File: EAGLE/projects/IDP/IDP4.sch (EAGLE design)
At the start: 14 parts, among them IC1 LM348P, M1 IDP_PROTOBOARD, U1 LM393P

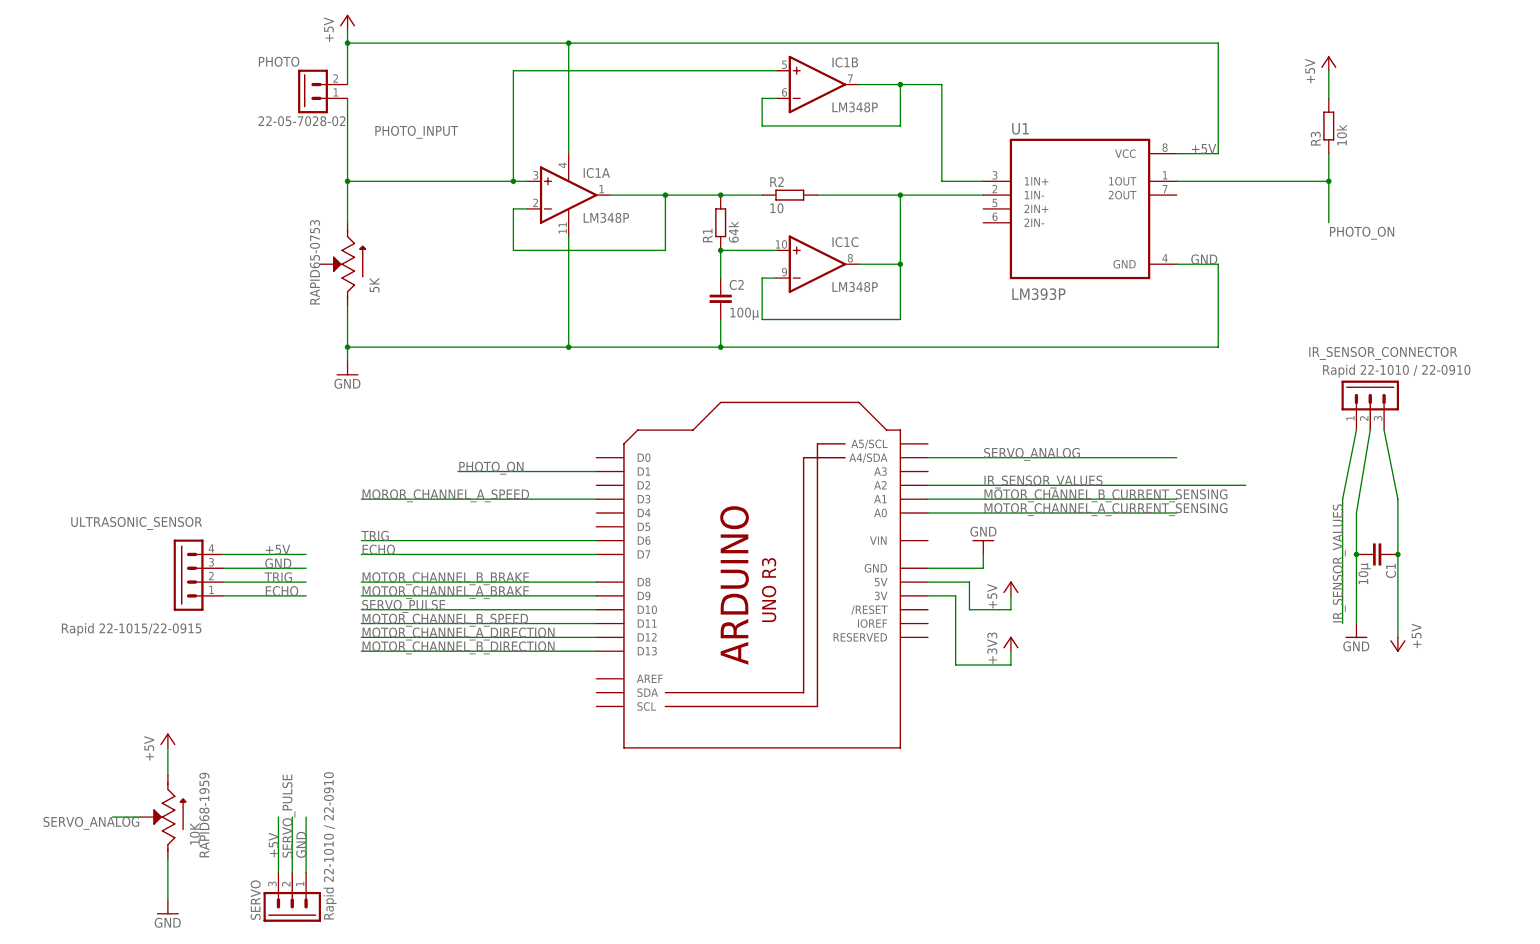
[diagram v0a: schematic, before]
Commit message: Added LED :+1:
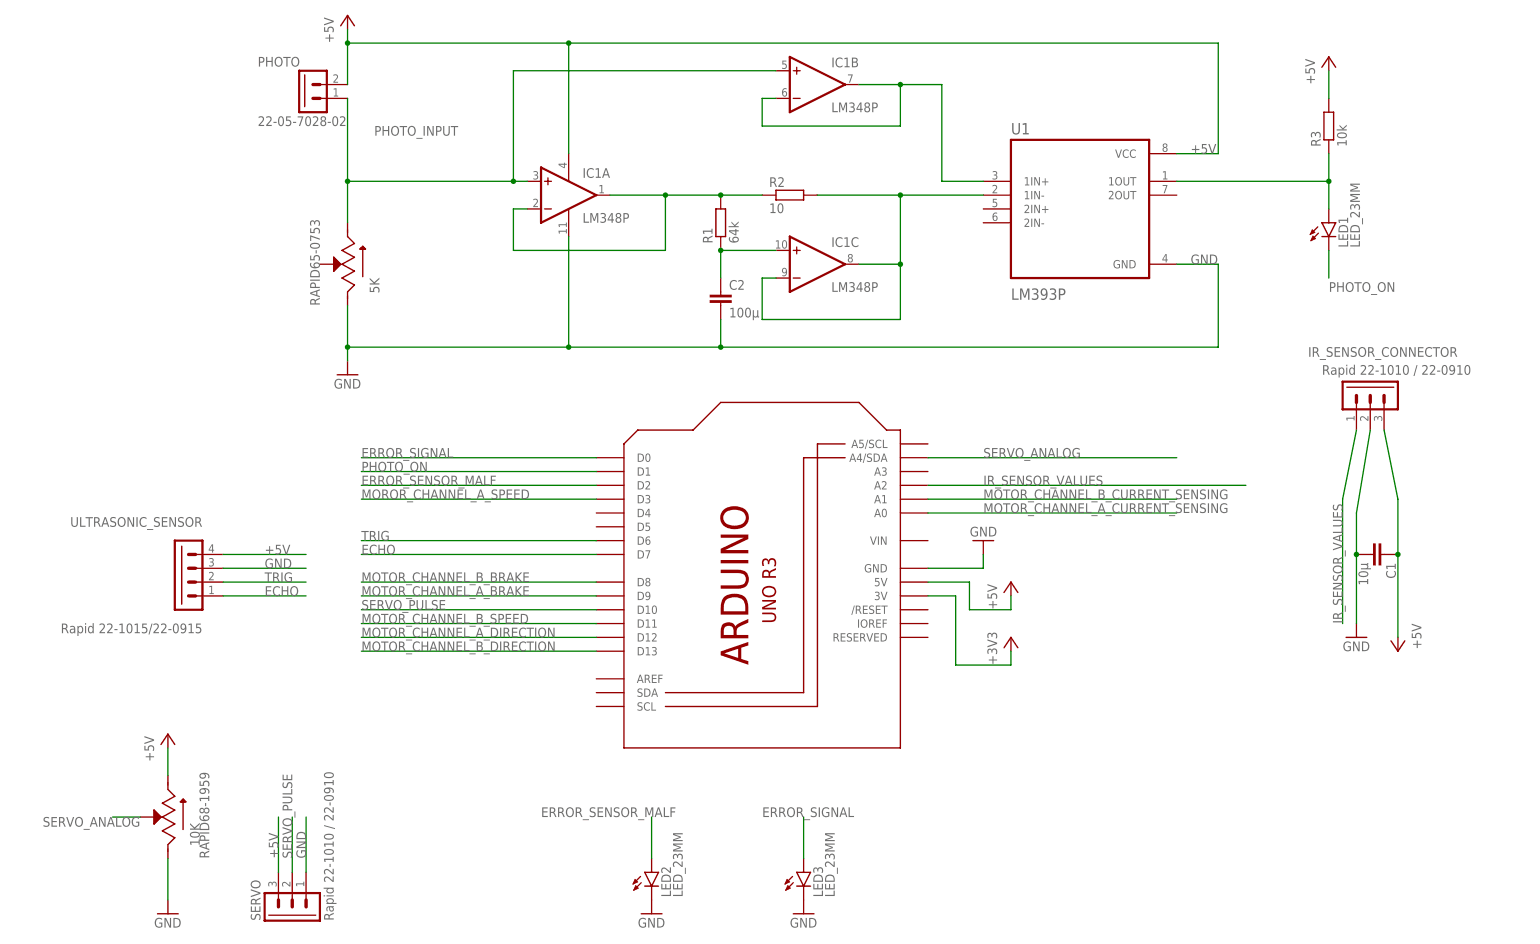
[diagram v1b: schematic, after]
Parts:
- added LED1, LED2, LED3: LED_23MM, IDP_library:LED_23MM
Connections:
- new net ERROR_SENSOR_MALF: LED2.A, M1.D2
- new net ERROR_SIGNAL: LED3.A, M1.D0
- net GND: now also LED2.C, LED3.C
- net PHOTO_ON: now also LED1.A, LED1.C
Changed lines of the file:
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@@
 <grid distance="0.1" unitdist="inch" unit="inch" style="lines" multiple="1" display="no" altdistance="0.01" altunitdist="inch" altunit="inch"/>
 <layers>
-<layer number="1" name="Top" color="4" fill="1" visible="yes" active="no"/>
-<layer number="16" name="Bottom" color="1" fill="1" visible="yes" active="no"/>
-<layer number="17" name="Pads" color="2" fill="1" visible="yes" active="no"/>
-<layer number="18" name="Vias" color="2" fill="1" visible="yes" active="no"/>
-<layer number="19" name="Unrouted" color="6" fill="1" visible="yes" active="no"/>
-<layer number="20" name="Dimension" color="24" fill="1" visible="yes" active="no"/>
-<layer number="21" name="tPlace" color="7" fill="1" visible="yes" active="no"/>
-<layer number="22" name="bPlace" color="7" fill="1" visible="yes" active="no"/>
-<layer number="23" name="tOrigins" color="15" fill="1" visible="yes" active="no"/>
-<layer number="24" name="bOrigins" color="15" fill="1" visible="yes" active="no"/>
-<layer number="25" name="tNames" color="7" fill="1" visible="yes" active="no"/>
-<layer number="26" name="bNames" color="7" fill="1" visible="yes" active="no"/>
-<layer number="27" name="tValues" color="7" fill="1" visible="yes" active="no"/>
-<layer number="28" name="bValues" color="7" fill="1" visible="yes" active="no"/>
+<layer number="1" name="Top" color="4" fill="1" visible="no" active="no"/>
+<layer number="16" name="Bottom" color="1" fill="1" visible="no" active="no"/>
+<layer number="17" name="Pads" color="2" fill="1" visible="no" active="no"/>
+<layer number="18" name="Vias" color="2" fill="1" visible="no" active="no"/>
+<layer number="19" name="Unrouted" color="6" fill="1" visible="no" active="no"/>
+<layer number="20" name="Dimension" color="24" fill="1" visible="no" active="no"/>
+<layer number="21" name="tPlace" color="7" fill="1" visible="no" active="no"/>
+<layer number="22" name="bPlace" color="7" fill="1" visible="no" active="no"/>
+<layer number="23" name="tOrigins" color="15" fill="1" visible="no" active="no"/>
+<layer number="24" name="bOrigins" color="15" fill="1" visible="no" active="no"/>
+<layer number="25" name="tNames" color="7" fill="1" visible="no" active="no"/>
+<layer number="26" name="bNames" color="7" fill="1" visible="no" active="no"/>
+<layer number="27" name="tValues" color="7" fill="1" visible="no" active="no"/>
+<layer number="28" name="bValues" color="7" fill="1" visible="no" active="no"/>
 <layer number="29" name="tStop" color="7" fill="3" visible="no" active="no"/>
 <layer number="30" name="bStop" color="7" fill="6" visible="no" active="no"/>
@@
 <layer number="35" name="tGlue" color="7" fill="4" visible="no" active="no"/>
 <layer number="36" name="bGlue" color="7" fill="5" visible="no" active="no"/>
-<layer number="37" name="tTest" color="7" fill="1" visible="yes" active="no"/>
-<layer number="38" name="bTest" color="7" fill="1" visible="yes" active="no"/>
+<layer number="37" name="tTest" color="7" fill="1" visible="no" active="no"/>
+<layer number="38" name="bTest" color="7" fill="1" visible="no" active="no"/>
 <layer number="39" name="tKeepout" color="4" fill="11" visible="no" active="no"/>
 <layer number="40" name="bKeepout" color="1" fill="11" visible="no" active="no"/>
@@
 <layer number="44" name="Drills" color="7" fill="1" visible="no" active="no"/>
 <layer number="45" name="Holes" color="7" fill="1" visible="no" active="no"/>
-<layer number="46" name="Milling" color="3" fill="1" visible="yes" active="no"/>
-<layer number="47" name="Measures" color="7" fill="1" visible="yes" active="no"/>
-<layer number="48" name="Document" color="7" fill="1" visible="yes" active="no"/>
-<layer number="49" name="Reference" color="7" fill="1" visible="yes" active="no"/>
-<layer number="50" name="dxf" color="7" fill="1" visible="yes" active="no"/>
-<layer number="51" name="tDocu" color="7" fill="1" visible="yes" active="no"/>
-<layer number="52" name="bDocu" color="7" fill="1" visible="yes" active="no"/>
-<layer number="53" name="tGND_GNDA" color="7" fill="9" visible="yes" active="no"/>
-<layer number="54" name="bGND_GNDA" color="1" fill="9" visible="yes" active="no"/>
-<layer number="56" name="wert" color="7" fill="1" visible="yes" active="no"/>
-<layer number="57" name="tCAD" color="7" fill="1" visible="yes" active="no"/>
-<layer number="59" name="tCarbon" color="7" fill="1" visible="yes" active="no"/>
-<layer number="60" name="bCarbon" color="7" fill="1" visible="yes" active="no"/>
+<layer number="46" name="Milling" color="3" fill="1" visible="no" active="no"/>
+<layer number="47" name="Measures" color="7" fill="1" visible="no" active="no"/>
+<layer number="48" name="Document" color="7" fill="1" visible="no" active="no"/>
+<layer number="49" name="Reference" color="7" fill="1" visible="no" active="no"/>
+<layer number="50" name="dxf" color="7" fill="1" visible="no" active="no"/>
+<layer number="51" name="tDocu" color="7" fill="1" visible="no" active="no"/>
+<layer number="52" name="bDocu" color="7" fill="1" visible="no" active="no"/>
+<layer number="53" name="tGND_GNDA" color="7" fill="9" visible="no" active="no"/>
+<layer number="54" name="bGND_GNDA" color="1" fill="9" visible="no" active="no"/>
+<layer number="56" name="wert" color="7" fill="1" visible="no" active="no"/>
+<layer number="57" name="tCAD" color="7" fill="1" visible="no" active="no"/>
+<layer number="59" name="tCarbon" color="7" fill="1" visible="no" active="no"/>
+<layer number="60" name="bCarbon" color="7" fill="1" visible="no" active="no"/>
 <layer number="88" name="SimResults" color="9" fill="1" visible="yes" active="yes"/>
 <layer number="89" name="SimProbes" color="9" fill="1" visible="yes" active="yes"/>
@@
 <part name="P+4" library="IDP_library" deviceset="+5V" device=""/>
 <part name="R2" library="IDP_library" deviceset="R-EU_" device="0204/2V" package3d_urn="urn:adsk.eagle:package:23495/1" value="10"/>
+<part name="LED1" library="IDP_library" deviceset="LED_2" device="3MM" package3d_urn="urn:adsk.eagle:package:15797/1"/>
+<part name="LED2" library="IDP_library" deviceset="LED_2" device="3MM" package3d_urn="urn:adsk.eagle:package:15797/1"/>
+<part name="LED3" library="IDP_library" deviceset="LED_2" device="3MM" package3d_urn="urn:adsk.eagle:package:15797/1"/>
+<part name="GND5" library="IDP_library" deviceset="GND" device=""/>
+<part name="GND6" library="IDP_library" deviceset="GND" device=""/>
 </parts>
 <sheets>
@@
 <attribute name="NAME" x="184.15" y="131.0386" size="1.778" layer="95"/>
 <attribute name="VALUE" x="184.15" y="126.238" size="1.778" layer="96"/>
+</instance>
+<instance part="LED1" gate="G$1" x="287.02" y="124.46" smashed="yes">
+<attribute name="NAME" x="290.576" y="119.888" size="1.778" layer="95" rot="R90"/>
+<attribute name="VALUE" x="292.735" y="119.888" size="1.778" layer="96" rot="R90"/>
+</instance>
+<instance part="LED2" gate="G$1" x="162.56" y="5.08" smashed="yes">
+<attribute name="NAME" x="166.116" y="0.508" size="1.778" layer="95" rot="R90"/>
+<attribute name="VALUE" x="168.275" y="0.508" size="1.778" layer="96" rot="R90"/>
+</instance>
+<instance part="LED3" gate="G$1" x="190.5" y="5.08" smashed="yes">
+<attribute name="NAME" x="194.056" y="0.508" size="1.778" layer="95" rot="R90"/>
+<attribute name="VALUE" x="196.215" y="0.508" size="1.778" layer="96" rot="R90"/>
+</instance>
+<instance part="GND5" gate="1" x="162.56" y="-2.54" smashed="yes">
+<attribute name="VALUE" x="160.02" y="-5.08" size="1.778" layer="96"/>
+</instance>
+<instance part="GND6" gate="1" x="190.5" y="-2.54" smashed="yes">
+<attribute name="VALUE" x="187.96" y="-5.08" size="1.778" layer="96"/>
 </instance>
 </instances>
@@
 <label x="91.44" y="60.96" size="1.778" layer="95"/>
 </segment>
+<segment>
+<pinref part="LED2" gate="G$1" pin="C"/>
+<pinref part="GND5" gate="1" pin="GND"/>
+</segment>
+<segment>
+<pinref part="LED3" gate="G$1" pin="C"/>
+<pinref part="GND6" gate="1" pin="GND"/>
+</segment>
 </net>
 <net name="+3V3" class="0">
@@
 <segment>
 <pinref part="M1" gate="G$1" pin="D1"/>
-<wire x1="152.4" y1="78.74" x2="127" y2="78.74" width="0.1524" layer="91"/>
-<label x="127" y="78.74" size="1.778" layer="95"/>
+<wire x1="152.4" y1="78.74" x2="109.22" y2="78.74" width="0.1524" layer="91"/>
+<label x="109.22" y="78.74" size="1.778" layer="95"/>
 </segment>
 <segment>
 <pinref part="U1" gate="A" pin="1OUT"/>
 <wire x1="259.08" y1="132.08" x2="287.02" y2="132.08" width="0.1524" layer="91"/>
-<wire x1="287.02" y1="132.08" x2="287.02" y2="124.46" width="0.1524" layer="91"/>
 <wire x1="287.02" y1="132.08" x2="287.02" y2="137.16" width="0.1524" layer="91"/>
+<pinref part="R3" gate="G$1" pin="1"/>
+<pinref part="LED1" gate="G$1" pin="A"/>
+<wire x1="287.02" y1="132.08" x2="287.02" y2="127" width="0.1524" layer="91"/>
 <junction x="287.02" y="132.08"/>
-<pinref part="R3" gate="G$1" pin="1"/>
-<label x="287.02" y="121.92" size="1.778" layer="95"/>
+</segment>
+<segment>
+<pinref part="LED1" gate="G$1" pin="C"/>
+<wire x1="287.02" y1="119.38" x2="287.02" y2="114.3" width="0.1524" layer="91"/>
+<label x="287.02" y="111.76" size="1.778" layer="95"/>
 </segment>
 </net>
@@
 </segment>
 </net>
+<net name="ERROR_SIGNAL" class="0">
+<segment>
+<pinref part="M1" gate="G$1" pin="D0"/>
+<wire x1="152.4" y1="81.28" x2="109.22" y2="81.28" width="0.1524" layer="91"/>
+<label x="109.22" y="81.28" size="1.778" layer="95"/>
+</segment>
+<segment>
+<pinref part="LED3" gate="G$1" pin="A"/>
+<wire x1="190.5" y1="7.62" x2="190.5" y2="15.24" width="0.1524" layer="91"/>
+<label x="182.88" y="15.24" size="1.778" layer="95"/>
+</segment>
+</net>
+<net name="ERROR_SENSOR_MALF" class="0">
+<segment>
+<pinref part="M1" gate="G$1" pin="D2"/>
+<wire x1="152.4" y1="76.2" x2="109.22" y2="76.2" width="0.1524" layer="91"/>
+<label x="109.22" y="76.2" size="1.778" layer="95"/>
+</segment>
+<segment>
+<pinref part="LED2" gate="G$1" pin="A"/>
+<wire x1="162.56" y1="7.62" x2="162.56" y2="15.24" width="0.1524" layer="91"/>
+<label x="142.24" y="15.24" size="1.778" layer="95"/>
+</segment>
+</net>

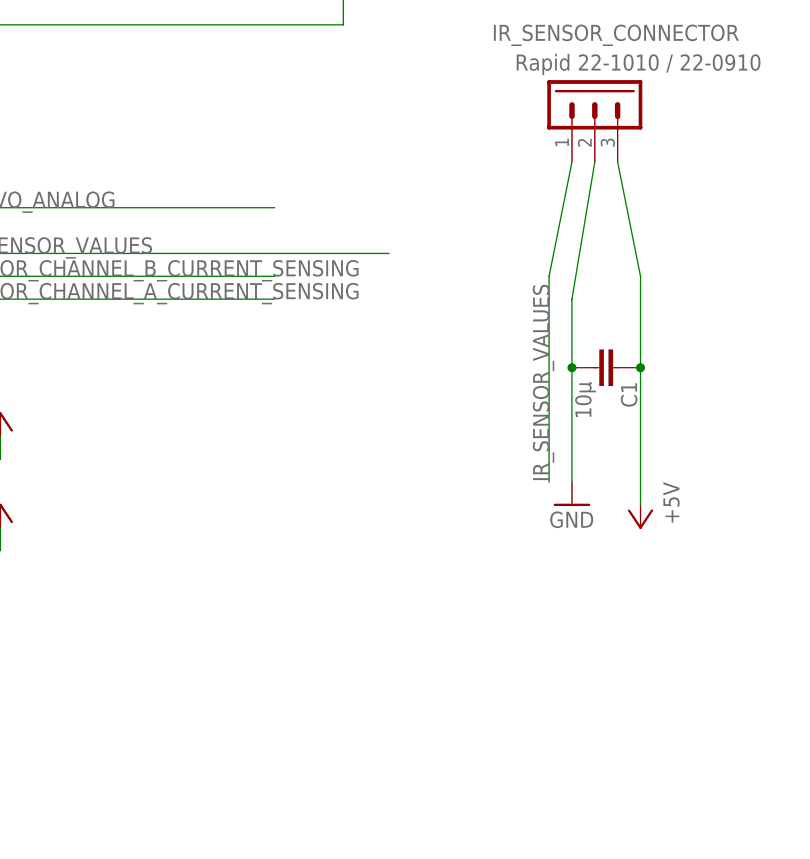
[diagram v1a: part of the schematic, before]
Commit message: Added low pass filter
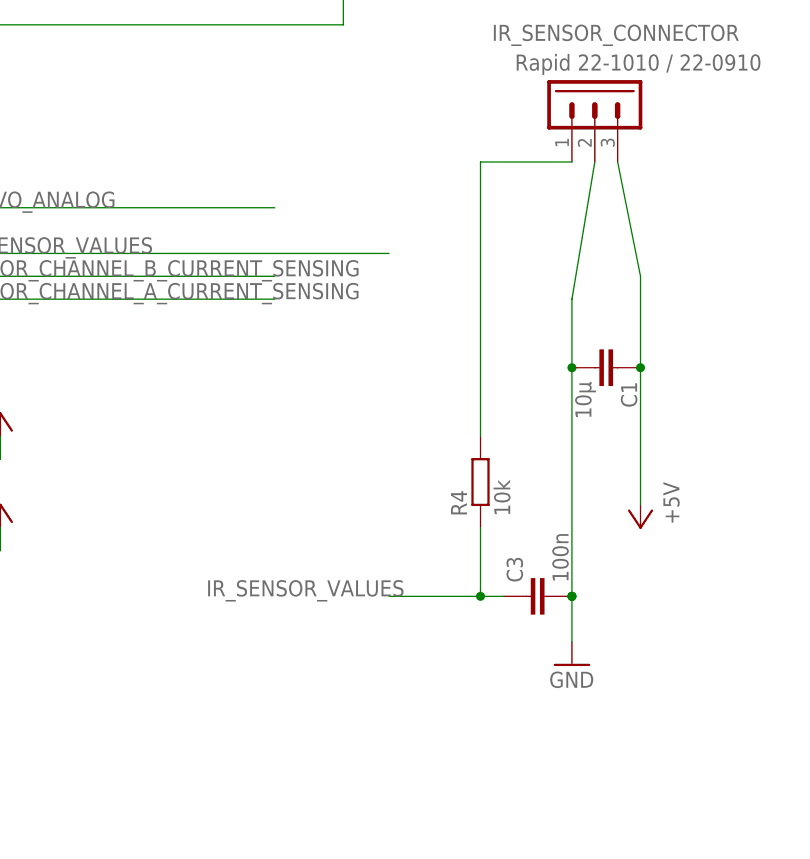
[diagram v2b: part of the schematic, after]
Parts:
- added C3: 100n, IDP_library:C-EU025-024X044
- added R4: 10k, IDP_library:R-EU_0204/7
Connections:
- new net N$5: IR_SENSOR_CONNECTOR.1, R4.2
- net GND: now also C3.2
- net IR_SENSOR_VALUES: now also C3.1, R4.1; no longer IR_SENSOR_CONNECTOR.1
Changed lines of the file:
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@@
 <part name="GND5" library="IDP_library" deviceset="GND" device=""/>
 <part name="GND6" library="IDP_library" deviceset="GND" device=""/>
+<part name="R4" library="IDP_library" deviceset="R-EU_" device="0204/7" package3d_urn="urn:adsk.eagle:package:23498/2" value="10k"/>
+<part name="C3" library="IDP_library" deviceset="C-EU" device="025-024X044" package3d_urn="urn:adsk.eagle:package:23630/1" value="100n"/>
 </parts>
 <sheets>
@@
 <attribute name="VALUE" x="302.26" y="50.8" size="1.778" layer="96" rot="R270"/>
 </instance>
-<instance part="GND2" gate="1" x="292.1" y="48.26" smashed="yes">
-<attribute name="VALUE" x="289.56" y="45.72" size="1.778" layer="96"/>
+<instance part="GND2" gate="1" x="292.1" y="30.48" smashed="yes">
+<attribute name="VALUE" x="289.56" y="27.94" size="1.778" layer="96"/>
 </instance>
 <instance part="ULTRASONIC_SENSOR" gate="G$1" x="76.2" y="60.96" smashed="yes">
@@
 <instance part="GND6" gate="1" x="190.5" y="-2.54" smashed="yes">
 <attribute name="VALUE" x="187.96" y="-5.08" size="1.778" layer="96"/>
+</instance>
+<instance part="R4" gate="G$1" x="281.94" y="50.8" smashed="yes" rot="R90">
+<attribute name="NAME" x="280.4414" y="46.99" size="1.778" layer="95" rot="R90"/>
+<attribute name="VALUE" x="285.242" y="46.99" size="1.778" layer="96" rot="R90"/>
+</instance>
+<instance part="C3" gate="G$1" x="287.02" y="38.1" smashed="yes" rot="R90">
+<attribute name="NAME" x="286.639" y="39.624" size="1.778" layer="95" rot="R90"/>
+<attribute name="VALUE" x="291.719" y="39.624" size="1.778" layer="96" rot="R90"/>
 </instance>
 </instances>
@@
 <wire x1="292.1" y1="63.5" x2="292.1" y2="71.12" width="0.1524" layer="91"/>
 <wire x1="292.1" y1="71.12" x2="294.64" y2="86.36" width="0.1524" layer="91"/>
-<wire x1="292.1" y1="63.5" x2="292.1" y2="50.8" width="0.1524" layer="91"/>
+<wire x1="292.1" y1="63.5" x2="292.1" y2="38.1" width="0.1524" layer="91"/>
 <junction x="292.1" y="63.5"/>
 <pinref part="GND2" gate="1" pin="GND"/>
+<pinref part="C3" gate="G$1" pin="2"/>
+<wire x1="292.1" y1="38.1" x2="292.1" y2="33.02" width="0.1524" layer="91"/>
+<junction x="292.1" y="38.1"/>
 </segment>
 <segment>
@@
 </segment>
 <segment>
-<pinref part="IR_SENSOR_CONNECTOR" gate="G$1" pin="1"/>
-<wire x1="292.1" y1="86.36" x2="289.56" y2="73.66" width="0.1524" layer="91"/>
-<wire x1="289.56" y1="73.66" x2="289.56" y2="50.8" width="0.1524" layer="91"/>
-<label x="289.56" y="50.8" size="1.778" layer="95" rot="R90"/>
+<pinref part="R4" gate="G$1" pin="1"/>
+<wire x1="281.94" y1="45.72" x2="281.94" y2="38.1" width="0.1524" layer="91"/>
+<wire x1="281.94" y1="38.1" x2="271.78" y2="38.1" width="0.1524" layer="91"/>
+<pinref part="C3" gate="G$1" pin="1"/>
+<wire x1="281.94" y1="38.1" x2="284.48" y2="38.1" width="0.1524" layer="91"/>
+<junction x="281.94" y="38.1"/>
+<label x="251.46" y="38.1" size="1.778" layer="95"/>
 </segment>
 </net>
@@
 </segment>
 </net>
+<net name="N$5" class="0">
+<segment>
+<pinref part="IR_SENSOR_CONNECTOR" gate="G$1" pin="1"/>
+<wire x1="292.1" y1="86.36" x2="281.94" y2="86.36" width="0.1524" layer="91"/>
+<pinref part="R4" gate="G$1" pin="2"/>
+<wire x1="281.94" y1="86.36" x2="281.94" y2="55.88" width="0.1524" layer="91"/>
+</segment>
+</net>
+<net name="N$7" class="0">
+<segment>
+<junction x="292.1" y="38.1"/>
+</segment>
+</net>
